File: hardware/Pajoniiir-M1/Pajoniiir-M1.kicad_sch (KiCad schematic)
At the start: 0 parts

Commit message: hardware: capture Rev A input eFuse schematic
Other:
- sheet 01_POWER_INPUT ports: added 3V3_SYS, 5V_SYS, EFUSE_PG; removed none
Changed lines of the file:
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@@
       (effects (font (size 1.27 1.27)) (justify left top))
+    )
+    (pin "3V3_SYS" output
+      (at 20 25 180)
+      (effects (font (size 1.27 1.27)) (justify left))
+    )
+    (pin "5V_SYS" input
+      (at 65 25 0)
+      (effects (font (size 1.27 1.27)) (justify right))
+    )
+    (pin "EFUSE_PG" input
+      (at 65 30 0)
+      (effects (font (size 1.27 1.27)) (justify right))
     )
     (instances

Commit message: hardware: capture Rev A 3V3 system buck schematic
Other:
- sheet 02_POWER_3V3 ports: added 3V3_AUDIO, 3V3_C6, 3V3_PG, 3V3_SYS, 5V_SYS; removed none
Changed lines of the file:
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@@
       (effects (font (size 1.27 1.27)) (justify left top))
+    )
+    (pin "5V_SYS" output
+      (at 75 25 180)
+      (effects (font (size 1.27 1.27)) (justify left))
+    )
+    (pin "3V3_SYS" input
+      (at 120 23 0)
+      (effects (font (size 1.27 1.27)) (justify right))
+    )
+    (pin "3V3_PG" input
+      (at 120 27 0)
+      (effects (font (size 1.27 1.27)) (justify right))
+    )
+    (pin "3V3_C6" input
+      (at 120 31 0)
+      (effects (font (size 1.27 1.27)) (justify right))
+    )
+    (pin "3V3_AUDIO" input
+      (at 120 35 0)
+      (effects (font (size 1.27 1.27)) (justify right))
     )
     (instances
@@
     )
   )
+  (wire (pts (xy 65 25) (xy 75 25)) (stroke (width 0) (type default)))
   (sheet_instances (path "/" (page "1")))
   (embedded_fonts no)

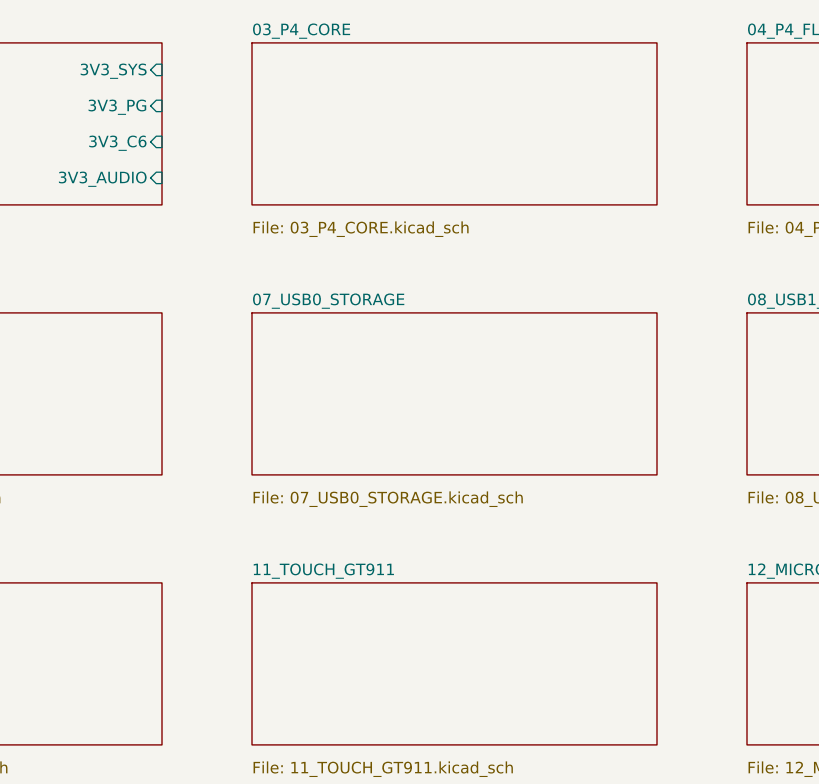
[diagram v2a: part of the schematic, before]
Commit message: hardware: capture ESP32-P4X v3 core and DCDC schematic
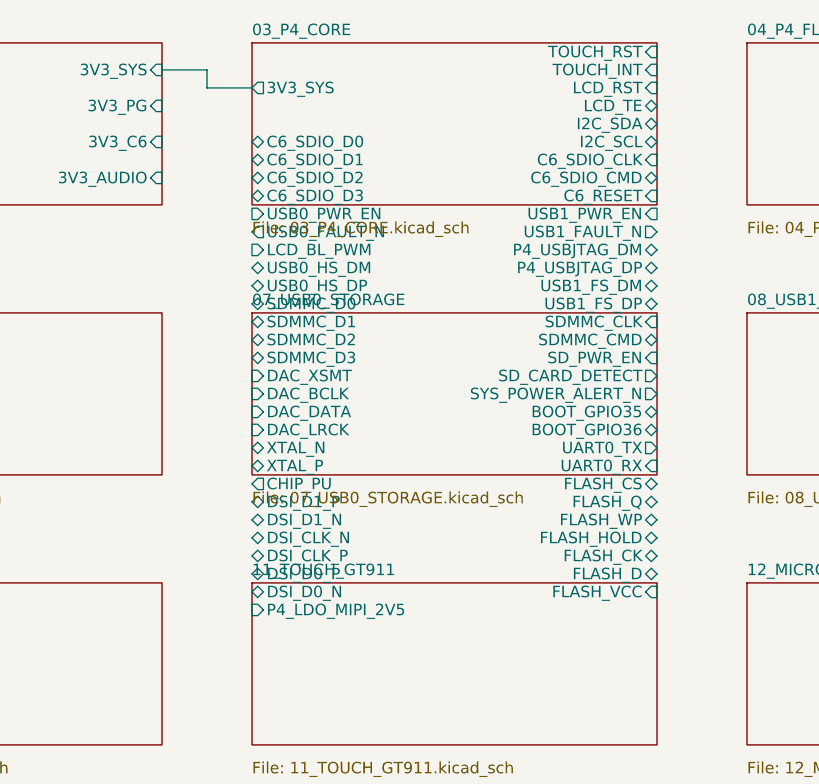
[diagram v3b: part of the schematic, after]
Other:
- sheet 03_P4_CORE ports: added 3V3_SYS, BOOT_GPIO35, BOOT_GPIO36, C6_RESET, C6_SDIO_CLK, C6_SDIO_CMD, C6_SDIO_D0, C6_SDIO_D1, C6_SDIO_D2, C6_SDIO_D3, CHIP_PU, DAC_BCLK, DAC_DATA, DAC_LRCK, DAC_XSMT, DSI_CLK_N, DSI_CLK_P, DSI_D0_N, DSI_D0_P, DSI_D1_N, DSI_D1_P, FLASH_CK, FLASH_CS, FLASH_D, FLASH_HOLD, FLASH_Q, FLASH_VCC, FLASH_WP, I2C_SCL, I2C_SDA, LCD_BL_PWM, LCD_RST, LCD_TE, P4_LDO_MIPI_2V5, P4_USBJTAG_DM, P4_USBJTAG_DP, SDMMC_CLK, SDMMC_CMD, SDMMC_D0, SDMMC_D1, SDMMC_D2, SDMMC_D3, SD_CARD_DETECT, SD_PWR_EN, SYS_POWER_ALERT_N, TOUCH_INT, TOUCH_RST, UART0_RX, UART0_TX, USB0_FAULT_N, USB0_HS_DM, USB0_HS_DP, USB0_PWR_EN, USB1_FAULT_N, USB1_FS_DM, USB1_FS_DP, USB1_PWR_EN, XTAL_N, XTAL_P; removed none
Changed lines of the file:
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@@
       (effects (font (size 1.27 1.27)) (justify left top))
     )
+    (pin "3V3_SYS" output (at 130 25 180) (effects (font (size 1.27 1.27)) (justify left)))
+    (pin "TOUCH_RST" input (at 175 21 0) (effects (font (size 1.27 1.27)) (justify right)))
+    (pin "TOUCH_INT" input (at 175 23 0) (effects (font (size 1.27 1.27)) (justify right)))
+    (pin "LCD_RST" input (at 175 25 0) (effects (font (size 1.27 1.27)) (justify right)))
+    (pin "LCD_TE" bidirectional (at 175 27 0) (effects (font (size 1.27 1.27)) (justify right)))
+    (pin "I2C_SDA" bidirectional (at 175 29 0) (effects (font (size 1.27 1.27)) (justify right)))
+    (pin "I2C_SCL" bidirectional (at 175 31 0) (effects (font (size 1.27 1.27)) (justify right)))
+    (pin "C6_SDIO_D0" bidirectional (at 130 31 180) (effects (font (size 1.27 1.27)) (justify left)))
+    (pin "C6_SDIO_D1" bidirectional (at 130 33 180) (effects (font (size 1.27 1.27)) (justify left)))
+    (pin "C6_SDIO_D2" bidirectional (at 130 35 180) (effects (font (size 1.27 1.27)) (justify left)))
+    (pin "C6_SDIO_D3" bidirectional (at 130 37 180) (effects (font (size 1.27 1.27)) (justify left)))
+    (pin "C6_SDIO_CLK" input (at 175 33 0) (effects (font (size 1.27 1.27)) (justify right)))
+    (pin "C6_SDIO_CMD" bidirectional (at 175 35 0) (effects (font (size 1.27 1.27)) (justify right)))
+    (pin "C6_RESET" input (at 175 37 0) (effects (font (size 1.27 1.27)) (justify right)))
+    (pin "USB0_PWR_EN" input (at 130 39 180) (effects (font (size 1.27 1.27)) (justify left)))
+    (pin "USB0_FAULT_N" output (at 130 41 180) (effects (font (size 1.27 1.27)) (justify left)))
+    (pin "USB1_PWR_EN" input (at 175 39 0) (effects (font (size 1.27 1.27)) (justify right)))
+    (pin "USB1_FAULT_N" output (at 175 41 0) (effects (font (size 1.27 1.27)) (justify right)))
+    (pin "LCD_BL_PWM" input (at 130 43 180) (effects (font (size 1.27 1.27)) (justify left)))
+    (pin "P4_USBJTAG_DM" bidirectional (at 175 43 0) (effects (font (size 1.27 1.27)) (justify right)))
+    (pin "P4_USBJTAG_DP" bidirectional (at 175 45 0) (effects (font (size 1.27 1.27)) (justify right)))
+    (pin "USB0_HS_DM" bidirectional (at 130 45 180) (effects (font (size 1.27 1.27)) (justify left)))
+    (pin "USB0_HS_DP" bidirectional (at 130 47 180) (effects (font (size 1.27 1.27)) (justify left)))
+    (pin "USB1_FS_DM" bidirectional (at 175 47 0) (effects (font (size 1.27 1.27)) (justify right)))
+    (pin "USB1_FS_DP" bidirectional (at 175 49 0) (effects (font (size 1.27 1.27)) (justify right)))
+    (pin "SDMMC_D0" bidirectional (at 130 49 180) (effects (font (size 1.27 1.27)) (justify left)))
+    (pin "SDMMC_D1" bidirectional (at 130 51 180) (effects (font (size 1.27 1.27)) (justify left)))
+    (pin "SDMMC_D2" bidirectional (at 130 53 180) (effects (font (size 1.27 1.27)) (justify left)))
+    (pin "SDMMC_D3" bidirectional (at 130 55 180) (effects (font (size 1.27 1.27)) (justify left)))
+    (pin "SDMMC_CLK" input (at 175 51 0) (effects (font (size 1.27 1.27)) (justify right)))
+    (pin "SDMMC_CMD" bidirectional (at 175 53 0) (effects (font (size 1.27 1.27)) (justify right)))
+    (pin "SD_PWR_EN" input (at 175 55 0) (effects (font (size 1.27 1.27)) (justify right)))
+    (pin "SD_CARD_DETECT" output (at 175 57 0) (effects (font (size 1.27 1.27)) (justify right)))
+    (pin "DAC_XSMT" input (at 130 57 180) (effects (font (size 1.27 1.27)) (justify left)))
+    (pin "DAC_BCLK" input (at 130 59 180) (effects (font (size 1.27 1.27)) (justify left)))
+    (pin "DAC_DATA" input (at 130 61 180) (effects (font (size 1.27 1.27)) (justify left)))
+    (pin "DAC_LRCK" input (at 130 63 180) (effects (font (size 1.27 1.27)) (justify left)))
+    (pin "SYS_POWER_ALERT_N" output (at 175 59 0) (effects (font (size 1.27 1.27)) (justify right)))
+    (pin "BOOT_GPIO35" bidirectional (at 175 61 0) (effects (font (size 1.27 1.27)) (justify right)))
+    (pin "BOOT_GPIO36" bidirectional (at 175 63 0) (effects (font (size 1.27 1.27)) (justify right)))
+    (pin "UART0_TX" output (at 175 65 0) (effects (font (size 1.27 1.27)) (justify right)))
+    (pin "UART0_RX" input (at 175 67 0) (effects (font (size 1.27 1.27)) (justify right)))
+    (pin "XTAL_N" bidirectional (at 130 65 180) (effects (font (size 1.27 1.27)) (justify left)))
+    (pin "XTAL_P" bidirectional (at 130 67 180) (effects (font (size 1.27 1.27)) (justify left)))
+    (pin "CHIP_PU" output (at 130 69 180) (effects (font (size 1.27 1.27)) (justify left)))
+    (pin "FLASH_CS" bidirectional (at 175 69 0) (effects (font (size 1.27 1.27)) (justify right)))
+    (pin "FLASH_Q" bidirectional (at 175 71 0) (effects (font (size 1.27 1.27)) (justify right)))
+    (pin "FLASH_WP" bidirectional (at 175 73 0) (effects (font (size 1.27 1.27)) (justify right)))
+    (pin "FLASH_HOLD" bidirectional (at 175 75 0) (effects (font (size 1.27 1.27)) (justify right)))
+    (pin "FLASH_CK" bidirectional (at 175 77 0) (effects (font (size 1.27 1.27)) (justify right)))
+    (pin "FLASH_D" bidirectional (at 175 79 0) (effects (font (size 1.27 1.27)) (justify right)))
+    (pin "FLASH_VCC" input (at 175 81 0) (effects (font (size 1.27 1.27)) (justify right)))
+    (pin "DSI_D1_P" bidirectional (at 130 71 180) (effects (font (size 1.27 1.27)) (justify left)))
+    (pin "DSI_D1_N" bidirectional (at 130 73 180) (effects (font (size 1.27 1.27)) (justify left)))
+    (pin "DSI_CLK_N" bidirectional (at 130 75 180) (effects (font (size 1.27 1.27)) (justify left)))
+    (pin "DSI_CLK_P" bidirectional (at 130 77 180) (effects (font (size 1.27 1.27)) (justify left)))
+    (pin "DSI_D0_P" bidirectional (at 130 79 180) (effects (font (size 1.27 1.27)) (justify left)))
+    (pin "DSI_D0_N" bidirectional (at 130 81 180) (effects (font (size 1.27 1.27)) (justify left)))
+    (pin "P4_LDO_MIPI_2V5" input (at 130 83 180) (effects (font (size 1.27 1.27)) (justify left)))
     (instances
       (project "Pajoniiir-M1"
@@
   )
   (wire (pts (xy 65 25) (xy 75 25)) (stroke (width 0) (type default)))
+  (wire (pts (xy 120 23) (xy 125 23) (xy 125 25) (xy 130 25)) (stroke (width 0) (type default)))
   (sheet_instances (path "/" (page "1")))
   (embedded_fonts no)
